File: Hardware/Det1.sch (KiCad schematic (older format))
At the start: 46 parts, among them U1 MAX4477, U2 MAX4477, U5 MAX4477

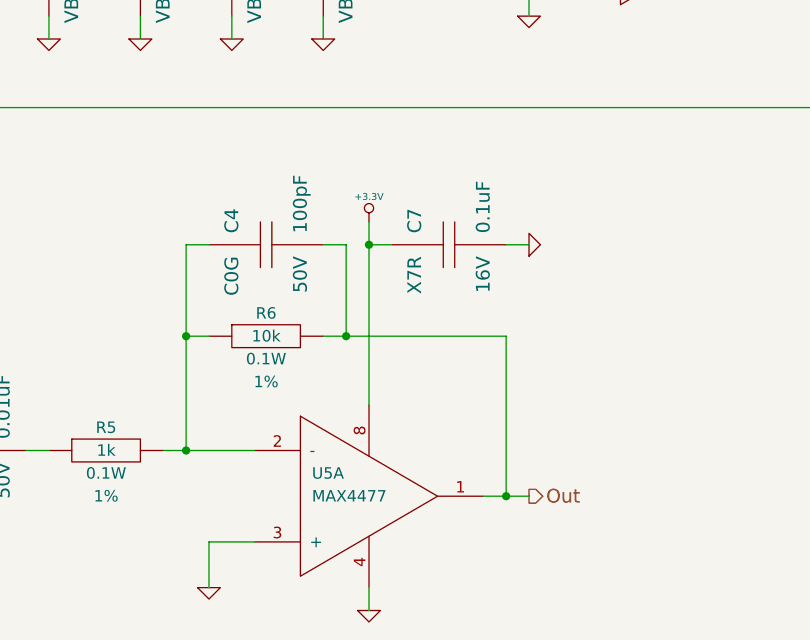
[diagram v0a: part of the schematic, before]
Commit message: New signal chain layout
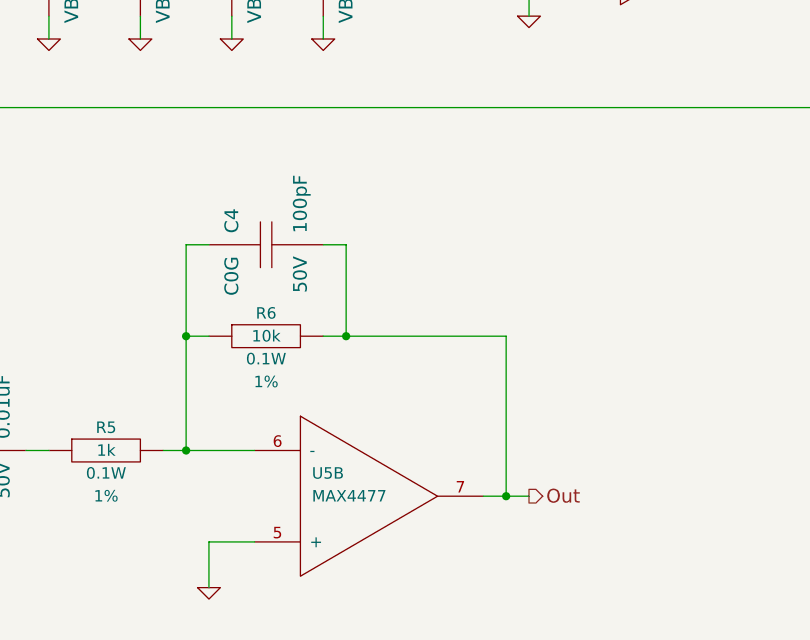
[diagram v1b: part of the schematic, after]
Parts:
- removed C7: 0.1uF, CAPC1608, symbol C
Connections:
- net +3.3V: no longer U5.8
- net GND: now also U5.5 (+); no longer U5.3 (+), U5.4
- net Out: now also U5.7; no longer U5.1
- net at C4.1, R5.2, R6.1: now also U5.6 (-); no longer U5.2 (-)
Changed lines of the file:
@@
 Sheet 2 5
 Title "Solid State Cosmic Ray Detector"
-Date "24 dec 2013"
+Date "26 dec 2013"
 Rev "1"
 Comp "Ethan Harstad"
@@
 	4700 5900 4700 6300
 Connection ~ 4700 6300
+Connection ~ 5400 7000
 $Comp
 L GND #PWR029
-U 1 1 52B947FF
-P 5500 5900
-F 0 "#PWR029" H 5500 5900 30  0001 C CNN
-F 1 "GND" H 5500 5830 30  0001 C CNN
-F 2 "" H 5500 5900 60  0000 C CNN
-F 3 "" H 5500 5900 60  0000 C CNN
-	1    5500 5900
-	0    -1   -1   0
-$EndComp
-Wire Wire Line
-	5500 5900 5400 5900
-Wire Wire Line
-	4800 5800 4800 6600
-Wire Wire Line
-	4900 5900 4800 5900
-Connection ~ 4800 5900
-Connection ~ 5400 7000
-$Comp
-L GND #PWR030
-U 1 1 52B9480B
-P 4800 7500
-F 0 "#PWR030" H 4800 7500 30  0001 C CNN
-F 1 "GND" H 4800 7430 30  0001 C CNN
-F 2 "" H 4800 7500 60  0000 C CNN
-F 3 "" H 4800 7500 60  0000 C CNN
-	1    4800 7500
-	1    0    0    -1
-$EndComp
-$Comp
-L GND #PWR031
 U 1 1 52B94811
 P 4100 7400
-F 0 "#PWR031" H 4100 7400 30  0001 C CNN
+F 0 "#PWR029" H 4100 7400 30  0001 C CNN
 F 1 "GND" H 4100 7330 30  0001 C CNN
 F 2 "" H 4100 7400 60  0000 C CNN
@@
 Wire Wire Line
 	4100 7200 4300 7200
-Wire Wire Line
-	4800 7400 4800 7500
 $Comp
 L OPAMP-DUAL U5
-U 1 1 52B9481D
+U 2 1 52B9481D
 P 4800 7000
 F 0 "U5" H 4550 7100 50  0000 L CNN
@@
 F 5 "MAX4477AUA+" H 4800 7000 60  0001 C CNN "MFR Part No"
 F 6 "MAX4477AUA+-ND" H 4800 7000 60  0001 C CNN "Distributor Part No"
-	1    4800 7000
+	2    4800 7000
 	1    0    0    -1
 $EndComp
@@
 	1    0    0    -1
 $EndComp
-$Comp
-L C C7
-U 1 1 52B94854
-P 5150 5900
-F 0 "C7" H 5200 6050 60  0000 L CNN
-F 1 "0.1uF" H 5200 5750 60  0000 L CNN
-F 2 "CAPC1608" H 5150 5900 60  0001 C CNN
-F 3 "~" H 5150 5900 60  0000 C CNN
-F 4 "Samsung" H 5150 5900 60  0001 C CNN "MFR Name"
-F 5 "CL10B104KO8NNNC" H 5150 5900 60  0001 C CNN "MFR Part No"
-F 6 "1276-1005-1-ND" H 5150 5900 60  0001 C CNN "Distributor Part No"
-F 7 "16V" H 5100 5750 60  0000 R CNN "Voltage"
-F 8 "X7R" H 5100 6050 60  0000 R CNN "Dielectric"
-	1    5150 5900
-	0    -1   -1   0
-$EndComp
-$Comp
-L +3.3V #PWR032
-U 1 1 52B9485A
-P 4800 5800
-F 0 "#PWR032" H 4800 5760 30  0001 C CNN
-F 1 "+3.3V" H 4800 5910 30  0000 C CNN
-F 2 "" H 4800 5800 60  0000 C CNN
-F 3 "" H 4800 5800 60  0000 C CNN
-	1    4800 5800
-	1    0    0    -1
-$EndComp

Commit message: Additional layout
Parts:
- added C45: 0.1uF, CAPC1608, symbol C
- added R13: 1M, RESC1608, symbol R
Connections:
- net +12V: now also R13.2
- net GND: now also C45.2
- net at C1.1, R1.1, R3.1: no longer R39.1
- new net: C45.1, R13.1, R39.1
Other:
- moved on the sheet: C1, R39
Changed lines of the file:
@@
 L GND #PWR06
 U 1 1 523D1DB5
-P 900 5000
-F 0 "#PWR06" H 900 5000 30  0001 C CNN
-F 1 "GND" H 900 4930 30  0001 C CNN
-F 2 "" H 900 5000 60  0000 C CNN
-F 3 "" H 900 5000 60  0000 C CNN
-	1    900  5000
+P 900 2600
+F 0 "#PWR06" H 900 2600 30  0001 C CNN
+F 1 "GND" H 900 2530 30  0001 C CNN
+F 2 "" H 900 2600 60  0000 C CNN
+F 3 "" H 900 2600 60  0000 C CNN
+	1    900  2600
 	1    0    0    -1
 $EndComp
@@
 L C C1
 U 1 1 52412D91
-P 900 4650
-F 0 "C1" H 950 4800 60  0000 L CNN
-F 1 "0.1uF" H 950 4500 60  0000 L CNN
-F 2 "CAPC1608" H 900 4650 60  0001 C CNN
-F 3 "~" H 900 4650 60  0000 C CNN
-F 4 "Samsung" H 900 4650 60  0001 C CNN "MFR Name"
-F 5 "CL10B104KO8NNNC" H 900 4650 60  0001 C CNN "MFR Part No"
-F 6 "1276-1005-1-ND" H 900 4650 60  0001 C CNN "Distributor Part No"
-F 7 "16V" H 850 4500 60  0000 R CNN "Voltage"
-F 8 "X7R" H 850 4800 60  0000 R CNN "Dielectric"
-	1    900  4650
+P 900 2250
+F 0 "C1" H 950 2400 60  0000 L CNN
+F 1 "0.1uF" H 950 2100 60  0000 L CNN
+F 2 "CAPC1608" H 900 2250 60  0001 C CNN
+F 3 "~" H 900 2250 60  0000 C CNN
+F 4 "Samsung" H 900 2250 60  0001 C CNN "MFR Name"
+F 5 "CL10B104KO8NNNC" H 900 2250 60  0001 C CNN "MFR Part No"
+F 6 "1276-1005-1-ND" H 900 2250 60  0001 C CNN "Distributor Part No"
+F 7 "16V" H 850 2100 60  0000 R CNN "Voltage"
+F 8 "X7R" H 850 2400 60  0000 R CNN "Dielectric"
+	1    900  2250
 	1    0    0    -1
 $EndComp
@@
 	3000 2500 3000 2600
 Wire Wire Line
-	900  5000 900  4900
+	900  2600 900  2500
 Wire Wire Line
 	900  1200 900  1300
-Wire Wire Line
-	900  1800 900  4400
 Wire Wire Line
 	1000 1900 900  1900
@@
 L R R39
 U 1 1 52B961DB
-P 1350 4300
-F 0 "R39" H 1350 4400 50  0000 C CNN
-F 1 "10M" H 1350 4300 50  0000 C CNN
-F 2 "RESC1608" H 1350 4300 60  0001 C CNN
-F 3 "~" H 1350 4300 60  0000 C CNN
-F 4 "Yageo" H 1350 4300 60  0001 C CNN "MFR Name"
-F 5 "RC0603FR-0710ML" H 1350 4300 60  0001 C CNN "MFR Part No"
-F 6 "311-10.0MHRCT-ND" H 1350 4300 60  0001 C CNN "Distributor Part No"
-F 7 "0.1W" H 1350 4200 50  0000 C CNN "Power"
-F 8 "1%" H 1350 4100 50  0000 C CNN "Tolerance"
-	1    1350 4300
-	1    0    0    -1
-$EndComp
-Wire Wire Line
-	1100 4300 900  4300
+P 1250 4300
+F 0 "R39" H 1250 4400 50  0000 C CNN
+F 1 "10M" H 1250 4300 50  0000 C CNN
+F 2 "RESC1608" H 1250 4300 60  0001 C CNN
+F 3 "~" H 1250 4300 60  0000 C CNN
+F 4 "Yageo" H 1250 4300 60  0001 C CNN "MFR Name"
+F 5 "RC0603FR-0710ML" H 1250 4300 60  0001 C CNN "MFR Part No"
+F 6 "311-10.0MHRCT-ND" H 1250 4300 60  0001 C CNN "Distributor Part No"
+F 7 "0.1W" H 1250 4200 50  0000 C CNN "Power"
+F 8 "1%" H 1250 4100 50  0000 C CNN "Tolerance"
+	1    1250 4300
+	1    0    0    -1
+$EndComp
+Wire Wire Line
+	1000 4300 900  4300
 Connection ~ 900  4300
 Wire Wire Line
-	1600 4300 4800 4300
+	1500 4300 4800 4300
 Text Label 4600 1800 1    60   ~ 0
 Det1A
 Text Label 4600 4200 1    60   ~ 0
 Det1B
+Wire Wire Line
+	900  1800 900  2000
+$Comp
+L R R13
+U 1 1 52BD5A23
+P 900 3950
+F 0 "R13" H 900 4050 50  0000 C CNN
+F 1 "1M" H 900 3950 50  0000 C CNN
+F 2 "RESC1608" H 900 3950 60  0001 C CNN
+F 3 "~" H 900 3950 60  0000 C CNN
+F 4 "Yageo" H 900 3950 60  0001 C CNN "MFR Name"
+F 5 "RC0603FR-071ML" H 900 3950 60  0001 C CNN "MFR Part No"
+F 6 "311-1.00MHRCT-ND" H 900 3950 60  0001 C CNN "Distributor Part No"
+F 7 "0.1W" H 900 3850 50  0000 C CNN "Power"
+F 8 "1%" H 900 3750 50  0000 C CNN "Tolerance"
+	1    900  3950
+	0    -1   -1   0
+$EndComp
+$Comp
+L C C45
+U 1 1 52BD5A2E
+P 900 4650
+F 0 "C45" H 950 4800 60  0000 L CNN
+F 1 "0.1uF" H 950 4500 60  0000 L CNN
+F 2 "CAPC1608" H 900 4650 60  0001 C CNN
+F 3 "~" H 900 4650 60  0000 C CNN
+F 4 "Samsung" H 900 4650 60  0001 C CNN "MFR Name"
+F 5 "CL10B104KO8NNNC" H 900 4650 60  0001 C CNN "MFR Part No"
+F 6 "1276-1005-1-ND" H 900 4650 60  0001 C CNN "Distributor Part No"
+F 7 "16V" H 850 4500 60  0000 R CNN "Voltage"
+F 8 "X7R" H 850 4800 60  0000 R CNN "Dielectric"
+	1    900  4650
+	1    0    0    -1
+$EndComp
+$Comp
+L GND #PWR030
+U 1 1 52BD5A4A
+P 900 5000
+F 0 "#PWR030" H 900 5000 30  0001 C CNN
+F 1 "GND" H 900 4930 30  0001 C CNN
+F 2 "" H 900 5000 60  0000 C CNN
+F 3 "" H 900 5000 60  0000 C CNN
+	1    900  5000
+	1    0    0    -1
+$EndComp
+$Comp
+L +12V #PWR031
+U 1 1 52BD5A59
+P 900 3600
+F 0 "#PWR031" H 900 3550 20  0001 C CNN
+F 1 "+12V" H 900 3700 30  0000 C CNN
+F 2 "" H 900 3600 60  0000 C CNN
+F 3 "" H 900 3600 60  0000 C CNN
+	1    900  3600
+	1    0    0    -1
+$EndComp
+Wire Wire Line
+	900  3600 900  3700
+Wire Wire Line
+	900  4200 900  4400
+Wire Wire Line
+	900  4900 900  5000
 $EndSCHEMATC

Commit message: Clear annotations
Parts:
- renumbered C1 to C?, C8 to C?, C10 to C?, C5 to C?, C6 to C?, C9 to C?, C11 to C?, C12 to C?, C2 to C?, C3 to C?, C15 to C?, C13 to C?, C14 to C?, C4 to C?, C45 to C?, D15 to D?, D13 to D?, D11 to D?, D9 to D?, D7 to D?, D5 to D?, D3 to D?, D1 to D?, D16 to D?, D14 to D?, D12 to D?, D10 to D?, D8 to D?, D6 to D?, D4 to D?, D2 to D?, R1 to R?, R3 to R?, R7 to R?, R8 to R?, R9 to R?, R4 to R?, R10 to R?, R11 to R?, R5 to R?, R6 to R?, R2 to R?, R39 to R?, R13 to R?, U1 to U?, U2 to U?, U5 to U?
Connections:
- net GND: now also U?.3 (+), U?.3 (+), U?.3 (+); no longer U?.5 (+), U?.5 (+), U?.5 (+)
- net Out: now also U?.1; no longer U?.7
- net at C?.1, C?.2, R?.1: now also U?.2 (-); no longer U?.6 (-)
- net at C?.1, C?.2, R?.2: now also U?.1; no longer U?.7 (x2)
- net at C?.1, R?.1, R?.2: now also U?.2 (-); no longer U?.6 (-) (x2)
